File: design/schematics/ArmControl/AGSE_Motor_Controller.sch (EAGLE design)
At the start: 7 parts, among them T1 2N3904, T2 2N3904

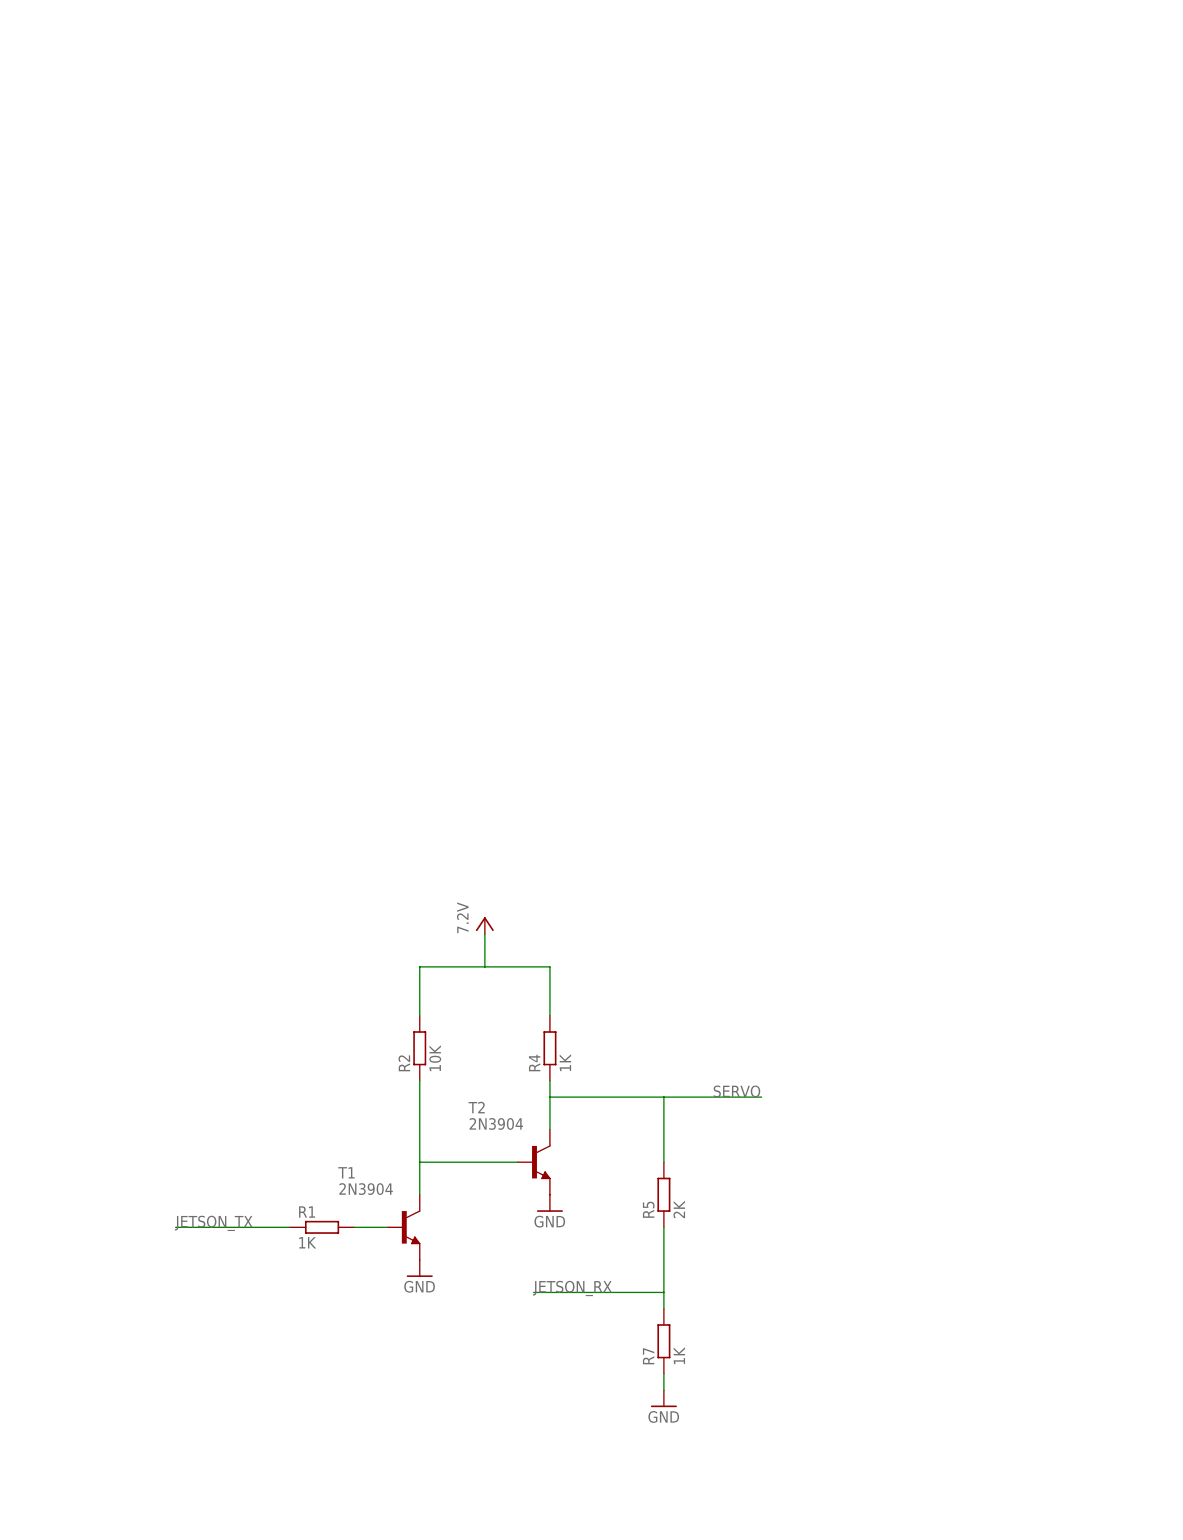
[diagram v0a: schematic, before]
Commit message: updated repo to match current impl
added schematics and pictures
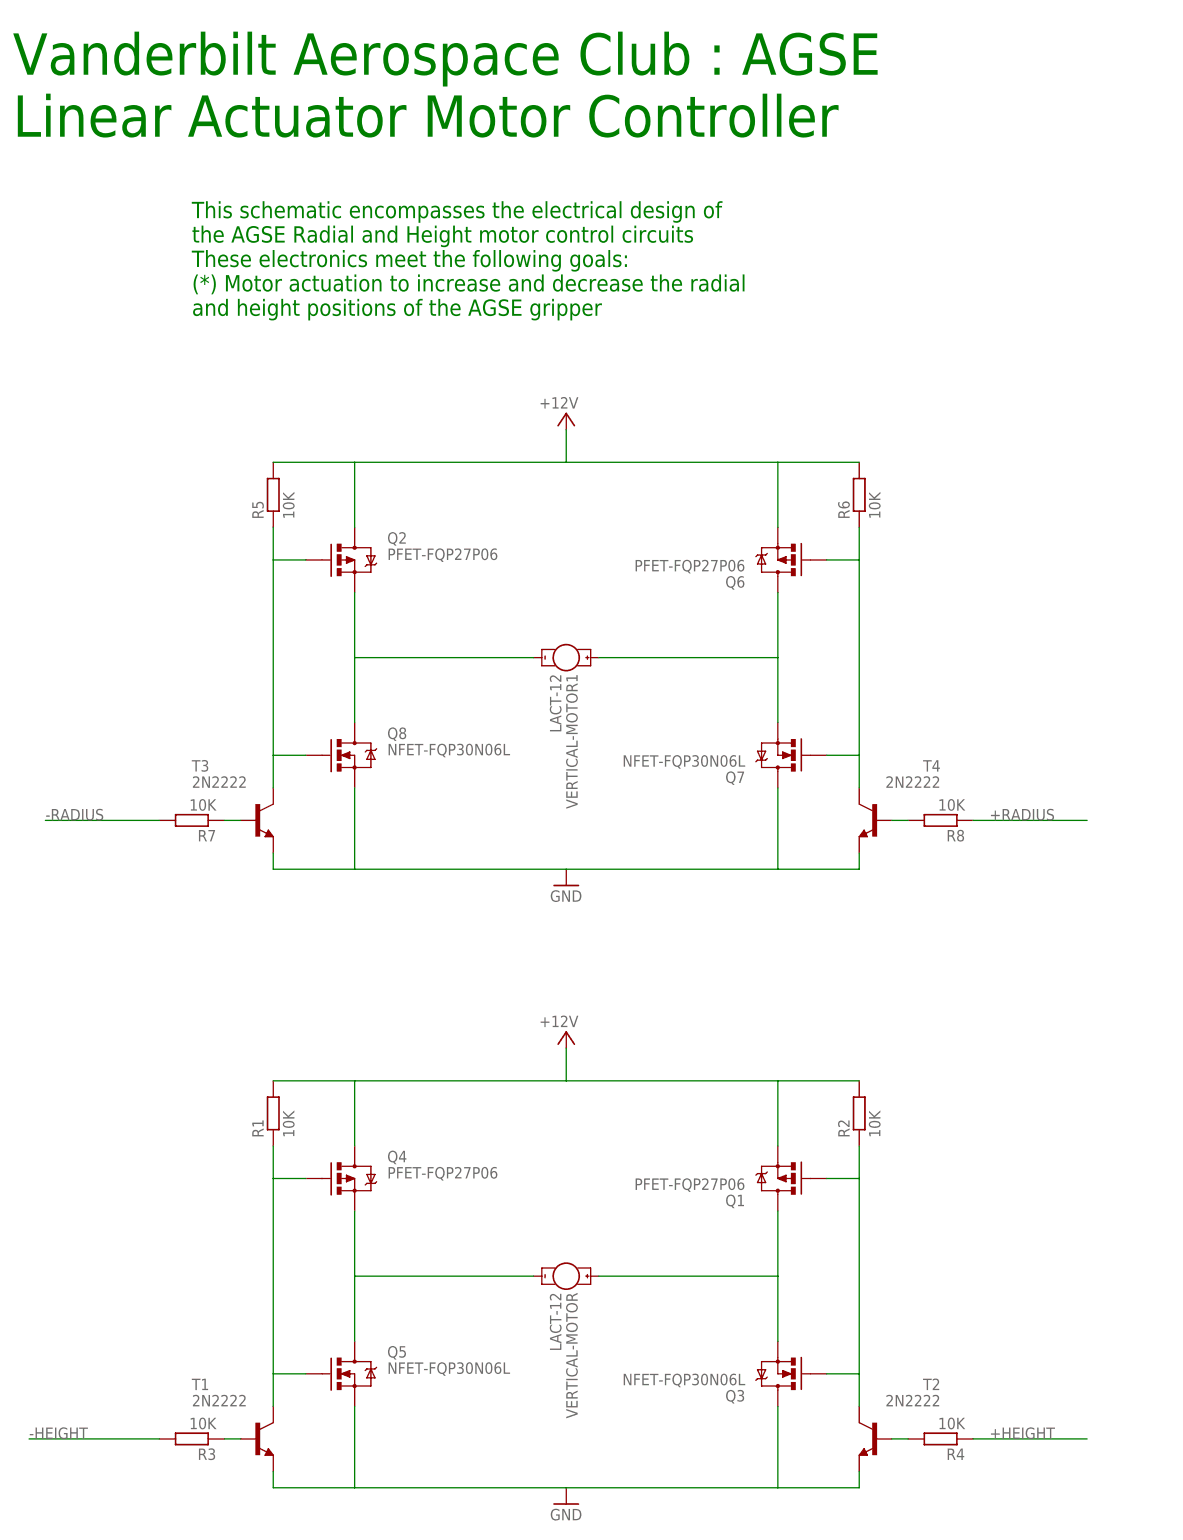
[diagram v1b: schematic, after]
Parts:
- added Q1, Q2, Q4, Q6: PFET-FQP27P06, SparkFun-DiscreteSemi:MOSFET-PCHANNELFQP27P06
- added Q3, Q5, Q7, Q8: NFET-FQP30N06L, SparkFun-DiscreteSemi:MOSFET-NCHANNELFQP30N06L
- added R3, R6, R8: 10K, resistor:R-EU_0207/12
- added T3, T4: 2N2222, transistor:2N2222
- added VERTICAL-MOTOR, VERTICAL-MOTOR1: LACT-12, SparkFun-Electromechanical:MOTOR10MM
- R1, R4, R7: value 1K -> 10K; device resistor:R-EU_0309/10 -> resistor:R-EU_0207/12
- R2: device resistor:R-EU_0309/10 -> resistor:R-EU_0207/12
- R5: value 2K -> 10K; device resistor:R-EU_0309/10 -> resistor:R-EU_0207/12
- T1, T2: value 2N3904 -> 2N2222; device transistor:2N3904 -> transistor:2N2222
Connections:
- removed net JETSON_RX: R5.1, R7.2
- removed net JETSON_TX: R1.1
- removed net SERVO: R4.1, R5.2, T2.C
- removed net VCC: R2.2, R4.2
- new net +5V: Q1.S, Q2.D, Q4.D, Q6.S, R1.2, R2.2, R5.2, R6.2
- new net +HEIGHT: R4.1
- new net +RADIUS: R8.1
- new net -HEIGHT: R3.2
- new net -RADIUS: R7.2
- new net N$10: Q6.G, Q7.G, R6.1, T4.C
- new net N$11: R7.1, T3.B
- new net N$12: R8.2, T4.B
- new net N$2: Q1.D, Q3.S, VERTICAL-MOTOR.+
- new net N$4: Q1.G, Q3.G, R2.1, T2.C
- new net N$5: R3.1, T1.B
- new net N$6: R4.2, T2.B
- new net N$7: Q6.D, Q7.S, VERTICAL-MOTOR1.+
- new net N$8: Q2.S, Q8.D, VERTICAL-MOTOR1.-
- new net N$9: Q2.G, Q8.G, R5.1, T3.C
- net GND: now also Q3.D, Q5.S, Q7.D, Q8.S, T3.E, T4.E; no longer R7.1
- net N$1: now also Q4.S, Q5.D, VERTICAL-MOTOR.-; no longer R1.2, T1.B
- net N$3: now also Q4.G, Q5.G, R1.1; no longer R2.1, T2.B
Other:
- note added: "This schematic encompasses the electrical design of the AGSE Radial and Height motor control circuits These electronics meet the following goals: (*) Motor actuation to increase and decrease the radial and height positions of the AGSE gripper"
- note added: "Vanderbilt Aerospace Club : AGSE Linear Actuator Motor Controller"
- moved on the sheet: R1, R2, R4, R5, R7
